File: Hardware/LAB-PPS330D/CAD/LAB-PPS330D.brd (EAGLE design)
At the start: 10.2 x 10.2 mm, 8 parts, among them J1 100mil, J2 100mil, U1 SN74LVC1G139, U2 ADP1196, U3 ADP1196, U4 ADP1196, U5 ADP1196, U6 SN74LVC3G04DCURBGA

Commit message: 1) This is the final Rev1 version going off to MFG
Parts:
- removed U5: ADP1196, My Library-adm:BGA6C40P2X3_90X138X64
- removed U6: SN74LVC3G04DCURBGA, My Library-adm:BGA8C50P2X4_190X90X50
- added R1: 1K, SparkFun-Resistors:0603-RES
- added V0, V1, V2: RED, SparkFun-LED:LED-0603
- U1: value SN74LVC1G139 -> SN74LVC1G139DCU; device My Library-adm:BGA8C50P2X4_190X90X50 -> LAB-PPS330D:SOP50P310X90-8N
- U2: value ADP1196 -> FDC6420C; device My Library-adm:BGA6C40P2X3_90X138X64 -> LAB-PPS330D:SOT95P270X145-6N
- U3, U4: value ADP1196 -> FDC6312P; device My Library-adm:BGA6C40P2X3_90X138X64 -> LAB-PPS330D:SOT95P270X145-6N
- moved U2 2.93 mm to (5.08, 1.91)
- moved U3 2.56 mm to (5.08, 5.08)
- moved U4 2.31 mm to (5.08, 8.26)
- moved U1 2.08 mm to (5.08, 5.08), flipped to the bottom, turned to 0 degrees
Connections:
- removed net N$3: U4.C1, U6.B1
- removed net N$4: U1.B2, U6.A1
- removed net N$6: U1.D2, U6.C2
- removed net N$7: U1.C1, U5.C1
- new net GNDS: U1.3, U2.1
- new net V0S: U1.7, U2.3, V0.C
- new net V1S: U1.6, U3.1, U3.3, V1.C
- new net V2S: U1.5, U4.1, U4.3, V2.C
- net DGND: now also U2.5; no longer U5.A1, U5.B1
- net N$1: now also U3.4, U3.6; no longer U2.C1, U6.B2
- net N$2: now also U4.4, U4.6; no longer U3.C1, U6.D2
- net N$5: now also R1.2, V0.A, V1.A, V2.A; no longer U1.C2, U6.C1
- net PE: now also U1.4, U2.6; no longer U1.D1, U2.C2, U3.C2, U4.C2, U5.A2, U5.B2, U5.C2, U6.D1
- net S0: now also J2.1, U1.1; no longer J2.3, U1.A1
- net S1: now also U1.2; no longer U1.B1
- net V0: now also R1.1, U1.8, U2.2; no longer U1.A2, U2.A1, U2.B1, U6.A2
- net V1: now also U3.5; no longer U3.A1, U3.B1
- net V2: now also U4.5; no longer U4.A1, U4.B1
- net VOUT: now also J2.3, U2.4, U3.2, U4.2; no longer J2.1, U2.A2, U2.B2, U3.A2, U3.B2, U4.A2, U4.B2
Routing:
- net V2S: track 0.00 -> 17.1 mm, vias 0 -> 1
- net V0S: track 0.00 -> 10.8 mm, vias 0 -> 1
- net V1S: track 0.00 -> 10.3 mm, vias 0 -> 1
- net N$1: track 12.5 -> 3.37 mm
- net GNDS: track 0.00 -> 6.25 mm, vias 0 -> 1
- net N$4: track 6.07 -> 0.00 mm
- net VOUT: track 20.8 -> 15.1 mm
- net S1: track 7.96 -> 2.81 mm
- net N$5: track 4.40 -> 9.31 mm, vias 0 -> 1
- net N$6: track 4.91 -> 0.00 mm
- net N$3: track 4.82 -> 0.00 mm, vias 2 -> 0
- net V0: track 14.2 -> 9.55 mm
- net V1: track 1.79 -> 6.08 mm, vias 0 -> 1
- net N$7: track 4.03 -> 0.00 mm, vias 2 -> 0
- net DGND: track 6.45 -> 2.70 mm
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- removed copper zone on layer 16, net PE
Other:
- board size 10.2 x 10.2 mm -> 12.4 x 10.2 mm
- board text added: "REV1"
- board text removed: "PPS330D"
- board text removed: "Rev0"

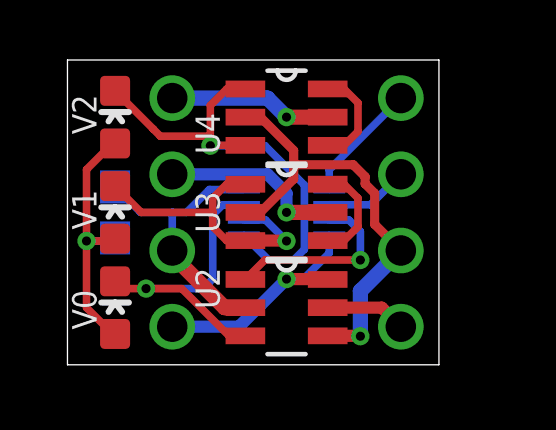
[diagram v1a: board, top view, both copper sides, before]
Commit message: 1) Shaved a few mils off .. this is the ACTUAL REV1
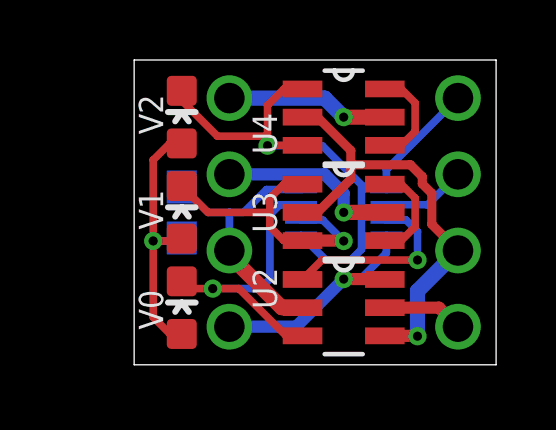
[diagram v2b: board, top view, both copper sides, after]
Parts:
- moved R1 2.22 mm to (1.59, 5.08)
- moved V0 2.22 mm to (1.59, 1.91)
- moved V1 2.22 mm to (1.59, 5.08)
- moved V2 2.22 mm to (1.59, 8.26)
- moved U1 1.91 mm to (6.99, 5.08)
- moved U2 1.91 mm to (6.99, 1.91)
- moved U3 1.91 mm to (6.99, 5.08)
- moved U4 1.91 mm to (6.99, 8.26)
- moved J1 1.90 mm to (3.17, 5.08)
- moved J2 1.90 mm to (10.8, 5.08)
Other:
- board size 12.4 x 10.2 mm -> 12.1 x 10.2 mm

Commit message: 1) Fixing the symbol / device for the FDC6420C MOSFET in the library. The symbol had the source/drain marked incorrectly though the device was pinned out correctly. 2) Because the symbol was wrong, I connected it wrong on the schematic ... So I fixed that 3) Then I fixed the layout to adjust for it. 4) Fixed the silkscreen had the signals on the bottom layer wrong. 5) Also adjusted the simulation to work correctly ... with the source and drain in the proper location for a low-side switch.
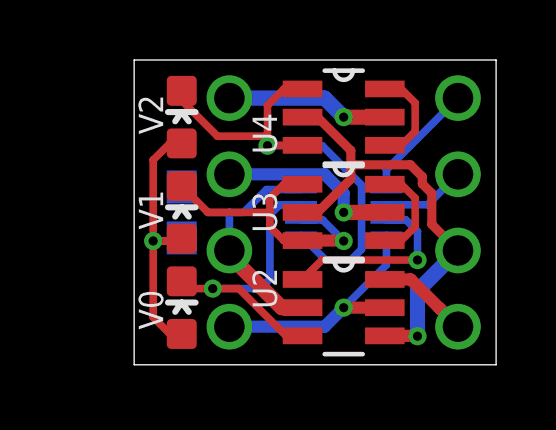
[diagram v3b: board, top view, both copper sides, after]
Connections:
- net DGND: now also U2.6; no longer U2.5
- net PE: now also U2.5; no longer U2.6
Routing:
- net DGND: track 2.70 -> 3.99 mm
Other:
- board text added: "REV2"
- board text removed: "REV1"
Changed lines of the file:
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@@
 <?xml version="1.0" encoding="utf-8"?>
 <!DOCTYPE eagle SYSTEM "eagle.dtd">
-<eagle version="6.6.0">
+<eagle version="6.5.0">
 <drawing>
 <settings>
@@
 <wire x1="12.065" y1="10.16" x2="0" y2="10.16" width="0" layer="20"/>
 <wire x1="0" y1="10.16" x2="0" y2="0" width="0" layer="20"/>
-<text x="8.6915625" y="7.540625" size="1.016" layer="26" rot="MR0">REV1</text>
+<text x="8.6915625" y="7.540625" size="1.016" layer="26" rot="MR0">REV2</text>
 <text x="4.28625" y="9.604375" size="0.8128" layer="26" rot="MR180">V2</text>
-<text x="6.429375" y="9.4853125" size="0.8128" layer="26" rot="MR180">VOUT</text>
+<text x="6.50875" y="3.1353125" size="0.8128" layer="26" rot="MR180">VOUT</text>
 <text x="4.28625" y="1.11125" size="0.8128" layer="26" rot="MR180">GND</text>
 <text x="8.255" y="7.14375" size="0.8128" layer="26" rot="MR180">S1</text>
-<text x="8.255" y="3.571875" size="0.8128" layer="26" rot="MR180">S0</text>
+<text x="8.175625" y="9.68375" size="0.8128" layer="26" rot="MR180">S0</text>
 <text x="4.3259375" y="7.1834375" size="0.8128" layer="26" rot="MR180">V1</text>
 <text x="4.28625" y="3.8496875" size="0.8128" layer="26" rot="MR180">V0</text>
-<text x="9.604375" y="1.349375" size="0.8128" layer="26" rot="MR0">DGND</text>
+<text x="9.36625" y="1.27" size="0.8128" layer="26" rot="MR0">DGND</text>
 </plain>
 <attributes>
@@
 <contactref element="J1" pad="4"/>
 <contactref element="U1" pad="4"/>
-<via x="6.985" y="2.8575" extent="1-16" drill="0.3048"/>
-<contactref element="U2" pad="6"/>
-<wire x1="8.3566" y1="2.8448" x2="7.9248" y2="2.8448" width="0.254" layer="1"/>
-<wire x1="8.4074" y1="4.318" x2="8.4074" y2="3.724275" width="0.254" layer="16"/>
-<wire x1="8.4074" y1="3.724275" x2="7.540625" y2="2.8575" width="0.254" layer="16"/>
-<wire x1="7.540625" y1="2.8575" x2="6.985" y2="2.8575" width="0.254" layer="16"/>
-<wire x1="6.985" y1="2.8575" x2="8.3439" y2="2.8575" width="0.4064" layer="1"/>
-<wire x1="8.3439" y1="2.8575" x2="8.3566" y2="2.8448" width="0.254" layer="1"/>
-<wire x1="6.985" y1="2.8575" x2="5.3975" y2="1.27" width="0.4064" layer="16"/>
-<wire x1="5.3975" y1="1.27" x2="3.175" y2="1.27" width="0.4064" layer="16"/>
+<via x="6.985" y="1.905" extent="1-16" drill="0.3048"/>
+<wire x1="6.35" y1="1.27" x2="3.175" y2="1.27" width="0.4064" layer="16"/>
+<contactref element="U2" pad="5"/>
+<wire x1="6.985" y1="1.905" x2="8.3566" y2="1.905" width="0.4064" layer="1"/>
+<wire x1="6.35" y1="1.27" x2="6.985" y2="1.905" width="0.4064" layer="16"/>
+<wire x1="6.985" y1="1.905" x2="8.4074" y2="3.3274" width="0.254" layer="16"/>
+<wire x1="8.4074" y1="3.3274" x2="8.4074" y2="4.318" width="0.254" layer="16"/>
 </signal>
 <signal name="V0">
@@
 <signal name="DGND">
 <contactref element="J2" pad="4"/>
-<contactref element="U2" pad="5"/>
-<wire x1="8.3566" y1="1.905" x2="10.16" y2="1.905" width="0.4064" layer="1"/>
 <wire x1="10.16" y1="1.905" x2="10.795" y2="1.27" width="0.4064" layer="1"/>
+<contactref element="U2" pad="6"/>
+<wire x1="8.3566" y1="2.8448" x2="9.2202" y2="2.8448" width="0.4064" layer="1"/>
+<wire x1="9.2202" y1="2.8448" x2="10.795" y2="1.27" width="0.4064" layer="1"/>
 </signal>
 <signal name="V0S">

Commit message: 1) Fixing the pinout on the PPS330D to match what is on the DEB429A -- the select lines are still off though. 2) Updating the BOM for the PLR5010D -- adding the base resistor for the BJTs
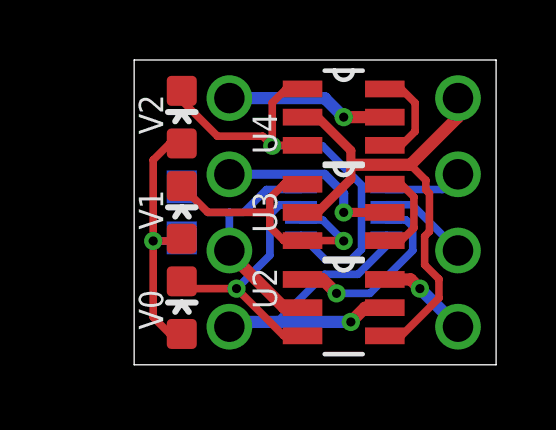
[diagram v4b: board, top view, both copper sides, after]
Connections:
- net S0: now also J2.2; no longer J2.1
- net S1: now also J2.3; no longer J2.2
- net VOUT: now also J2.1; no longer J2.3
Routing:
- net VOUT: track 15.1 -> 17.3 mm, vias 1 -> 0
- net PE: track 8.45 -> 10.5 mm
- net S0: track 4.04 -> 2.60 mm
- net V0S: track 10.4 -> 9.12 mm
- net DGND: track 3.99 -> 3.63 mm, vias 0 -> 1
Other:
- board text added: "REV3"
- board text removed: "REV2"
